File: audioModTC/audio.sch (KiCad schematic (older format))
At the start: 39 parts

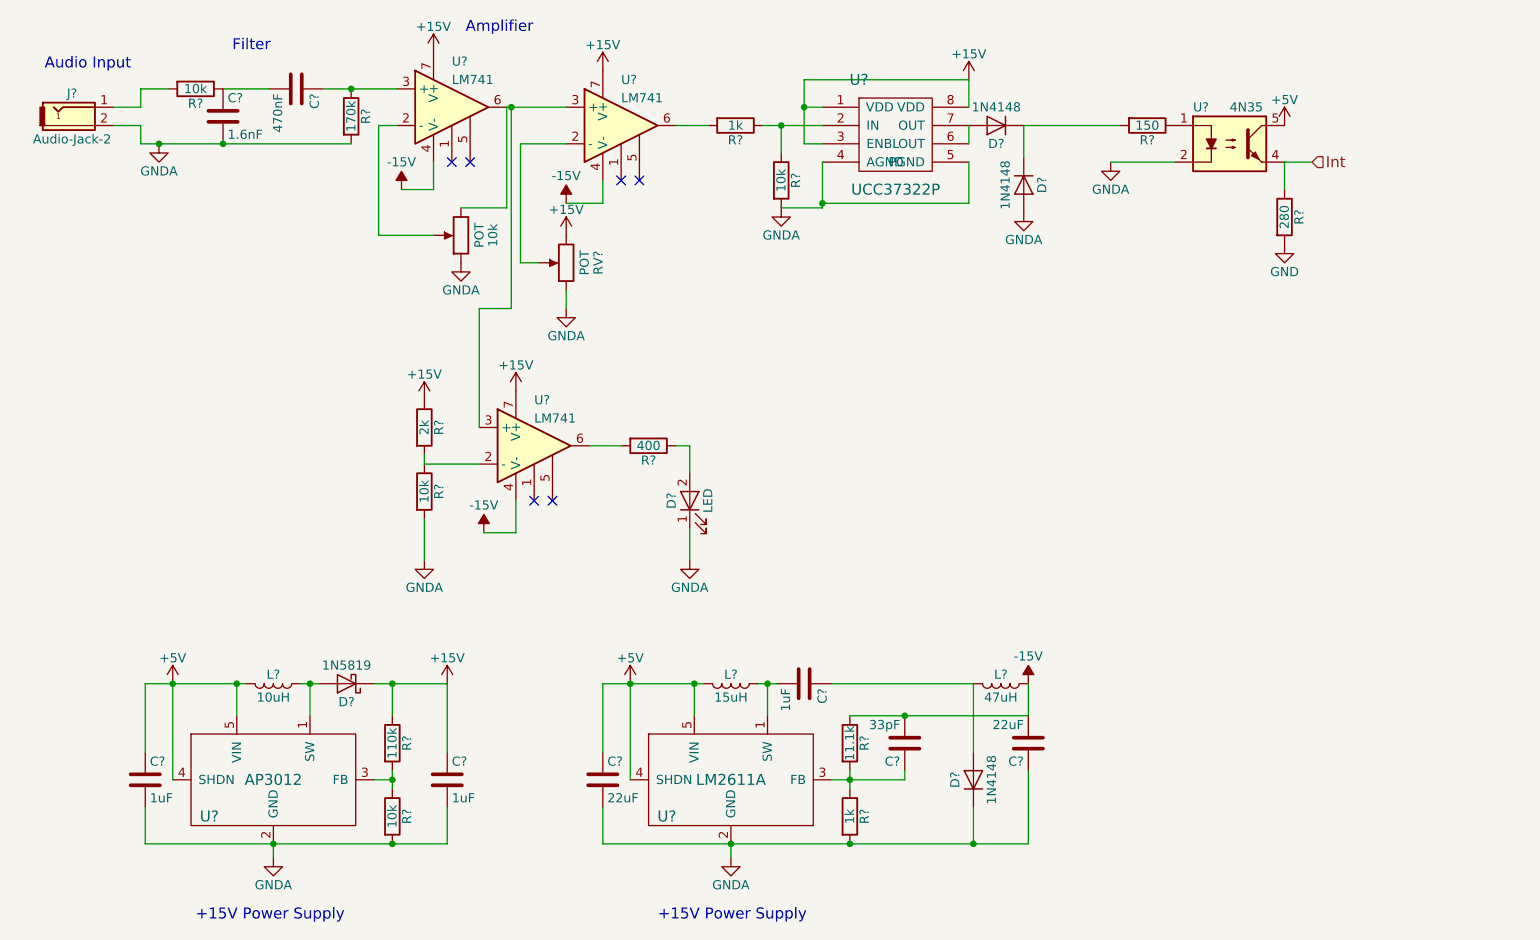
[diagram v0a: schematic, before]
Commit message: Made some footprints
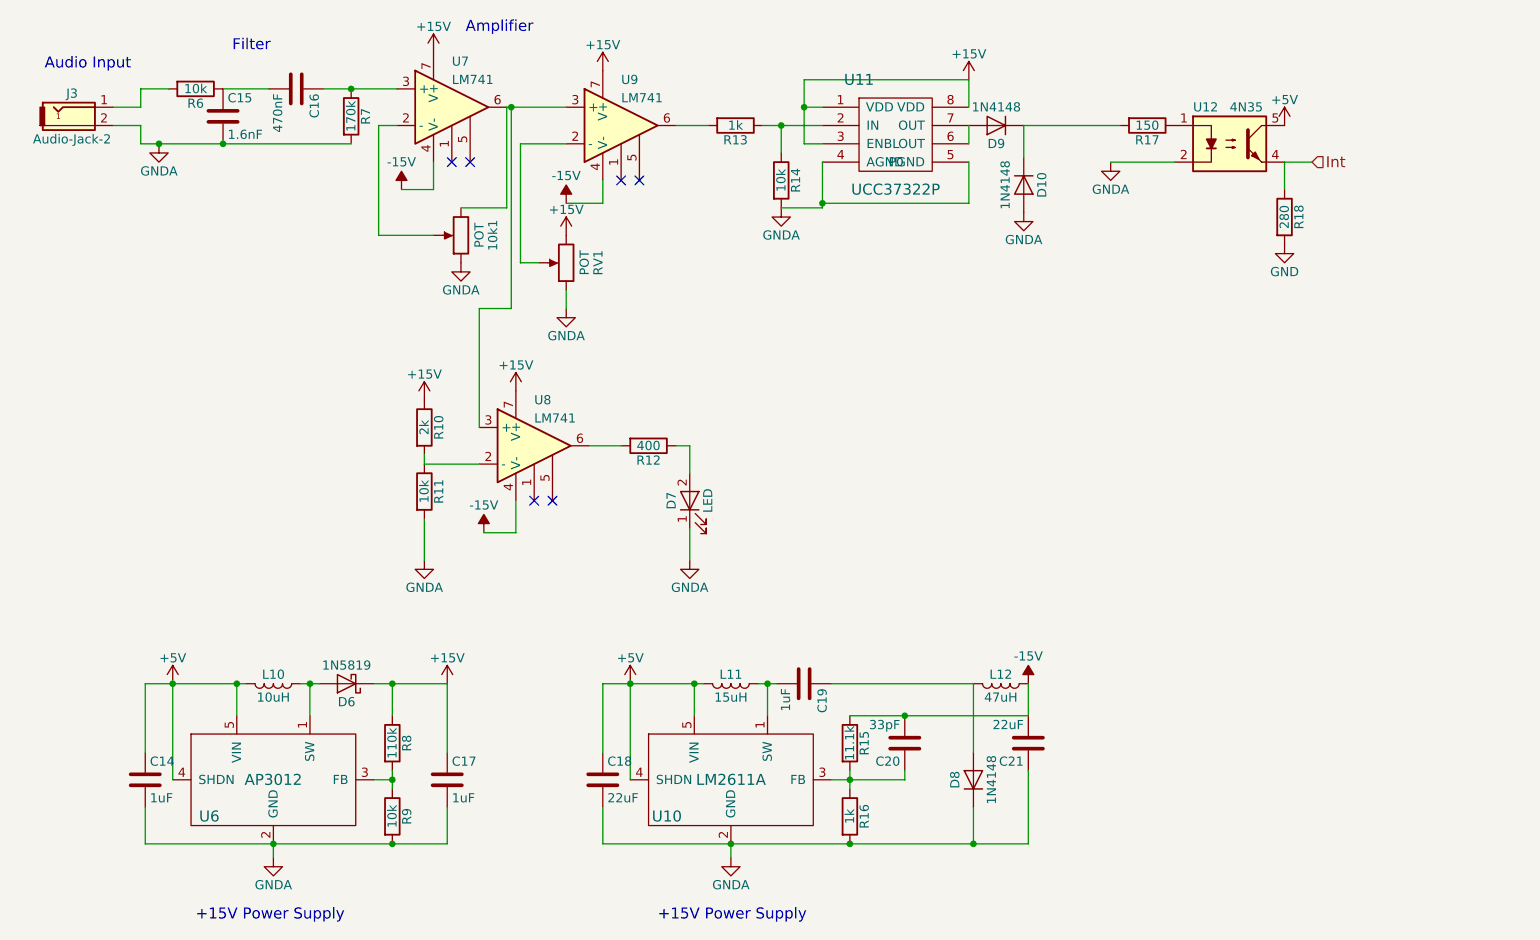
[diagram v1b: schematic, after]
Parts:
- C14, C15, C16, C17, C18, C19, C20, C21: renamed from C?; footprint (none) -> Capacitors_SMD:C_0603
- gave numbers to parts that had none: 30
- renumbered 10k to 10k1

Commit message: Assigned more footprints
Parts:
- D10, D8, D9: footprint (none) -> Diodes_SMD:D_SOD-323
- D6: footprint (none) -> Diodes_SMD:D_SOD-123
- D7: footprint (none) -> Diodes_SMD:D_0805
- J3: footprint (none) -> Custom:MJ1-2503A
- L10, L11, L12: footprint (none) -> Custom:L_1008
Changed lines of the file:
@@
 F 0 "D9" H 6925 2350 50  0000 C CNN
 F 1 "1N4148" H 6925 2150 50  0000 C CNN
-F 2 "" H 6925 2250 50  0001 C CNN
+F 2 "Diodes_SMD:D_SOD-323" H 6925 2250 50  0001 C CNN
 F 3 "" H 6925 2250 50  0001 C CNN
 	1    6925 2250
@@
 F 0 "D10" H 7075 2675 50  0000 C CNN
 F 1 "1N4148" H 7075 2475 50  0000 C CNN
-F 2 "" H 7075 2575 50  0001 C CNN
+F 2 "Diodes_SMD:D_SOD-323" H 7075 2575 50  0001 C CNN
 F 3 "" H 7075 2575 50  0001 C CNN
 	1    7075 2575
@@
 F 0 "D7" H 5250 4400 50  0000 C CNN
 F 1 "LED" H 5250 4200 50  0000 C CNN
-F 2 "" H 5250 4300 50  0001 C CNN
+F 2 "Diodes_SMD:D_0805" H 5250 4300 50  0001 C CNN
 F 3 "" H 5250 4300 50  0001 C CNN
 	1    5250 4300
@@
 F 0 "L10" V 2925 5300 50  0000 C CNN
 F 1 "10uH" V 3050 5300 50  0000 C CNN
-F 2 "" H 2975 5300 50  0001 C CNN
+F 2 "Custom:L_1008" H 2975 5300 50  0001 C CNN
 F 3 "" H 2975 5300 50  0001 C CNN
 	1    2975 5300
@@
 F 0 "D6" H 3375 5400 50  0000 C CNN
 F 1 "1N5819" H 3375 5200 50  0000 C CNN
-F 2 "" H 3375 5300 50  0001 C CNN
+F 2 "Diodes_SMD:D_SOD-123" H 3375 5300 50  0001 C CNN
 F 3 "" H 3375 5300 50  0001 C CNN
 	1    3375 5300
@@
 F 0 "L11" V 5425 5300 50  0000 C CNN
 F 1 "15uH" V 5550 5300 50  0000 C CNN
-F 2 "" H 5475 5300 50  0001 C CNN
+F 2 "Custom:L_1008" H 5475 5300 50  0001 C CNN
 F 3 "" H 5475 5300 50  0001 C CNN
 	1    5475 5300
@@
 F 0 "D8" H 6800 5925 50  0000 C CNN
 F 1 "1N4148" H 6800 5725 50  0000 C CNN
-F 2 "" H 6800 5825 50  0001 C CNN
+F 2 "Diodes_SMD:D_SOD-323" H 6800 5825 50  0001 C CNN
 F 3 "" H 6800 5825 50  0001 C CNN
 	1    6800 5825
@@
 F 0 "L12" V 6900 5300 50  0000 C CNN
 F 1 "47uH" V 7025 5300 50  0000 C CNN
-F 2 "" H 6950 5300 50  0001 C CNN
+F 2 "Custom:L_1008" H 6950 5300 50  0001 C CNN
 F 3 "" H 6950 5300 50  0001 C CNN
 	1    6950 5300
@@
 F 0 "J3" H 1875 2225 50  0000 C CNN
 F 1 "Audio-Jack-2" H 1875 1975 50  0000 C CNN
-F 2 "" H 2150 2150 50  0001 C CNN
+F 2 "Custom:MJ1-2503A" H 2150 2150 50  0001 C CNN
 F 3 "" H 2150 2150 50  0001 C CNN
 	1    1900 2150

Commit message: Made more footprints
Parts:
- R10, R11, R12, R13, R14, R15, R16, R17, R18, R6, R7, R8, R9: footprint (none) -> Resistors_SMD:R_0603
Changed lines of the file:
@@
 F 0 "R6" V 2630 2050 50  0000 C CNN
 F 1 "10k" V 2550 2050 50  0000 C CNN
-F 2 "" V 2480 2050 50  0001 C CNN
+F 2 "Resistors_SMD:R_0603" V 2480 2050 50  0001 C CNN
 F 3 "" H 2550 2050 50  0001 C CNN
 	1    2550 2050
@@
 F 0 "R7" V 3480 2200 50  0000 C CNN
 F 1 "170k" V 3400 2200 50  0000 C CNN
-F 2 "" V 3330 2200 50  0001 C CNN
+F 2 "Resistors_SMD:R_0603" V 3330 2200 50  0001 C CNN
 F 3 "" H 3400 2200 50  0001 C CNN
 	1    3400 2200
@@
 F 0 "R13" V 5580 2250 50  0000 C CNN
 F 1 "1k" V 5500 2250 50  0000 C CNN
-F 2 "" V 5430 2250 50  0001 C CNN
+F 2 "Resistors_SMD:R_0603" V 5430 2250 50  0001 C CNN
 F 3 "" H 5500 2250 50  0001 C CNN
 	1    5500 2250
@@
 F 0 "R14" V 5830 2550 50  0000 C CNN
 F 1 "10k" V 5750 2550 50  0000 C CNN
-F 2 "" V 5680 2550 50  0001 C CNN
+F 2 "Resistors_SMD:R_0603" V 5680 2550 50  0001 C CNN
 F 3 "" H 5750 2550 50  0001 C CNN
 	1    5750 2550
@@
 F 0 "R17" V 7830 2250 50  0000 C CNN
 F 1 "150" V 7750 2250 50  0000 C CNN
-F 2 "" V 7680 2250 50  0001 C CNN
+F 2 "Resistors_SMD:R_0603" V 7680 2250 50  0001 C CNN
 F 3 "" H 7750 2250 50  0001 C CNN
 	1    7750 2250
@@
 F 0 "R18" V 8580 2750 50  0000 C CNN
 F 1 "280" V 8500 2750 50  0000 C CNN
-F 2 "" V 8430 2750 50  0001 C CNN
+F 2 "Resistors_SMD:R_0603" V 8430 2750 50  0001 C CNN
 F 3 "" H 8500 2750 50  0001 C CNN
 	1    8500 2750
@@
 F 0 "R10" V 3880 3900 50  0000 C CNN
 F 1 "2k" V 3800 3900 50  0000 C CNN
-F 2 "" V 3730 3900 50  0001 C CNN
+F 2 "Resistors_SMD:R_0603" V 3730 3900 50  0001 C CNN
 F 3 "" H 3800 3900 50  0001 C CNN
 	1    3800 3900
@@
 F 0 "R11" V 3880 4250 50  0000 C CNN
 F 1 "10k" V 3800 4250 50  0000 C CNN
-F 2 "" V 3730 4250 50  0001 C CNN
+F 2 "Resistors_SMD:R_0603" V 3730 4250 50  0001 C CNN
 F 3 "" H 3800 4250 50  0001 C CNN
 	1    3800 4250
@@
 F 0 "R12" V 5105 4000 50  0000 C CNN
 F 1 "400" V 5025 4000 50  0000 C CNN
-F 2 "" V 4955 4000 50  0001 C CNN
+F 2 "Resistors_SMD:R_0603" V 4955 4000 50  0001 C CNN
 F 3 "" H 5025 4000 50  0001 C CNN
 	1    5025 4000
@@
 F 0 "R8" V 3705 5625 50  0000 C CNN
 F 1 "110k" V 3625 5625 50  0000 C CNN
-F 2 "" V 3555 5625 50  0001 C CNN
+F 2 "Resistors_SMD:R_0603" V 3555 5625 50  0001 C CNN
 F 3 "" H 3625 5625 50  0001 C CNN
 	1    3625 5625
@@
 F 0 "R9" V 3705 6025 50  0000 C CNN
 F 1 "10k" V 3625 6025 50  0000 C CNN
-F 2 "" V 3555 6025 50  0001 C CNN
+F 2 "Resistors_SMD:R_0603" V 3555 6025 50  0001 C CNN
 F 3 "" H 3625 6025 50  0001 C CNN
 	1    3625 6025
@@
 F 0 "R15" V 6205 5625 50  0000 C CNN
 F 1 "11.1k" V 6125 5625 50  0000 C CNN
-F 2 "" V 6055 5625 50  0001 C CNN
+F 2 "Resistors_SMD:R_0603" V 6055 5625 50  0001 C CNN
 F 3 "" H 6125 5625 50  0001 C CNN
 	1    6125 5625
@@
 F 0 "R16" V 6205 6025 50  0000 C CNN
 F 1 "1k" V 6125 6025 50  0000 C CNN
-F 2 "" V 6055 6025 50  0001 C CNN
+F 2 "Resistors_SMD:R_0603" V 6055 6025 50  0001 C CNN
 F 3 "" H 6125 6025 50  0001 C CNN
 	1    6125 6025

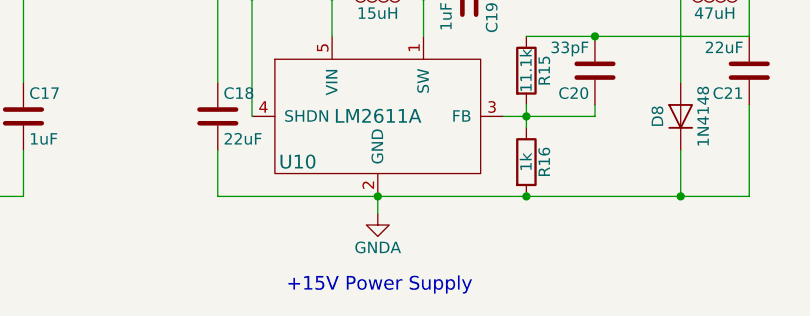
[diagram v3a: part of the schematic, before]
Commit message: Finished footprints
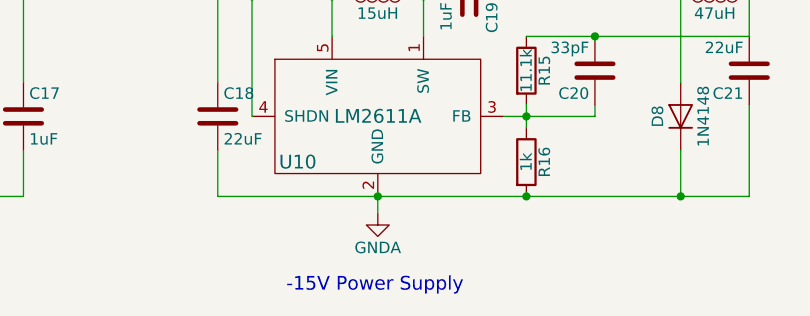
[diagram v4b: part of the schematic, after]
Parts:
- 10k1, RV1: footprint (none) -> Custom:PDB181-K220K-103B
- U10, U6: footprint (none) -> TO_SOT_Packages_SMD:SOT-23-5
- U11, U7, U8, U9: footprint (none) -> Housings_DIP:DIP-8_W7.62mm
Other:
- note added: "-15V Power Supply"
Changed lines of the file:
@@
 $EndComp
 $Comp
-L GNDA #PWR014
+L GNDA #PWR016
 U 1 1 5A4B5095
 P 2350 2350
-F 0 "#PWR014" H 2350 2100 50  0001 C CNN
+F 0 "#PWR016" H 2350 2100 50  0001 C CNN
 F 1 "GNDA" H 2350 2200 50  0000 C CNN
 F 2 "" H 2350 2350 50  0001 C CNN
@@
 F 0 "U7" H 3950 2400 50  0000 L CNN
 F 1 "LM741" H 3950 2300 50  0000 L CNN
-F 2 "" H 4000 2200 50  0001 C CNN
+F 2 "Housings_DIP:DIP-8_W7.62mm" H 4000 2200 50  0001 C CNN
 F 3 "" H 4100 2300 50  0001 C CNN
 	1    3950 2150
@@
 $EndComp
 $Comp
-L +15V #PWR015
+L +15V #PWR017
 U 1 1 5A4B51BF
 P 3850 1850
-F 0 "#PWR015" H 3850 1700 50  0001 C CNN
+F 0 "#PWR017" H 3850 1700 50  0001 C CNN
 F 1 "+15V" H 3850 1990 50  0000 C CNN
 F 2 "" H 3850 1850 50  0001 C CNN
@@
 $EndComp
 $Comp
-L -15V #PWR17
+L -15V #PWR18
 U 1 1 5A4B51DD
 P 3675 2600
-F 0 "#PWR17" H 3675 2700 50  0001 C CNN
+F 0 "#PWR18" H 3675 2700 50  0001 C CNN
 F 1 "-15V" H 3675 2750 50  0000 C CNN
 F 2 "" H 3675 2600 50  0001 C CNN
@@
 F 0 "10k1" V 3825 2850 50  0000 C CNN
 F 1 "POT" V 3900 2850 50  0000 C CNN
-F 2 "" H 4000 2850 50  0001 C CNN
+F 2 "Custom:PDB181-K220K-103B" H 4000 2850 50  0001 C CNN
 F 3 "" H 4000 2850 50  0001 C CNN
 	1    4000 2850
@@
 $EndComp
 $Comp
-L GNDA #PWR016
+L GNDA #PWR018
 U 1 1 5A4B5315
 P 4000 3000
-F 0 "#PWR016" H 4000 2750 50  0001 C CNN
+F 0 "#PWR018" H 4000 2750 50  0001 C CNN
 F 1 "GNDA" H 4000 2850 50  0000 C CNN
 F 2 "" H 4000 3000 50  0001 C CNN
@@
 F 0 "U9" H 4875 2500 50  0000 L CNN
 F 1 "LM741" H 4875 2400 50  0000 L CNN
-F 2 "" H 4925 2300 50  0001 C CNN
+F 2 "Housings_DIP:DIP-8_W7.62mm" H 4925 2300 50  0001 C CNN
 F 3 "" H 5025 2400 50  0001 C CNN
 	1    4875 2250
@@
 $EndComp
 $Comp
-L +15V #PWR017
+L +15V #PWR019
 U 1 1 5A4B53D4
 P 4775 1950
-F 0 "#PWR017" H 4775 1800 50  0001 C CNN
+F 0 "#PWR019" H 4775 1800 50  0001 C CNN
 F 1 "+15V" H 4775 2090 50  0000 C CNN
 F 2 "" H 4775 1950 50  0001 C CNN
@@
 $EndComp
 $Comp
-L -15V #PWR25
+L -15V #PWR26
 U 1 1 5A4B53F4
 P 4575 2675
-F 0 "#PWR25" H 4575 2775 50  0001 C CNN
+F 0 "#PWR26" H 4575 2775 50  0001 C CNN
 F 1 "-15V" H 4575 2825 50  0000 C CNN
 F 2 "" H 4575 2675 50  0001 C CNN
@@
 F 0 "RV1" V 4400 3000 50  0000 C CNN
 F 1 "POT" V 4475 3000 50  0000 C CNN
-F 2 "" H 4575 3000 50  0001 C CNN
+F 2 "Custom:PDB181-K220K-103B" H 4575 3000 50  0001 C CNN
 F 3 "" H 4575 3000 50  0001 C CNN
 	1    4575 3000
@@
 $EndComp
 $Comp
-L +15V #PWR018
+L +15V #PWR020
 U 1 1 5A4BBE9C
 P 4575 2850
-F 0 "#PWR018" H 4575 2700 50  0001 C CNN
+F 0 "#PWR020" H 4575 2700 50  0001 C CNN
 F 1 "+15V" H 4575 2990 50  0000 C CNN
 F 2 "" H 4575 2850 50  0001 C CNN
@@
 $EndComp
 $Comp
-L GNDA #PWR019
+L GNDA #PWR021
 U 1 1 5A4BBEC0
 P 4575 3250
-F 0 "#PWR019" H 4575 3000 50  0001 C CNN
+F 0 "#PWR021" H 4575 3000 50  0001 C CNN
 F 1 "GNDA" H 4575 3100 50  0000 C CNN
 F 2 "" H 4575 3250 50  0001 C CNN
@@
 F 0 "U11" H 6175 2600 60  0000 C CNN
 F 1 "UCC37322P" H 6375 2000 60  0000 C CNN
-F 2 "" H 6325 2300 60  0001 C CNN
+F 2 "Housings_DIP:DIP-8_W7.62mm" H 6325 2300 60  0001 C CNN
 F 3 "" H 6325 2300 60  0001 C CNN
 	1    6375 2300
@@
 	5875 2150 5975 2150
 $Comp
-L +15V #PWR020
+L +15V #PWR022
 U 1 1 5A4BC5F0
 P 6775 2000
-F 0 "#PWR020" H 6775 1850 50  0001 C CNN
+F 0 "#PWR022" H 6775 1850 50  0001 C CNN
 F 1 "+15V" H 6775 2140 50  0000 C CNN
 F 2 "" H 6775 2000 50  0001 C CNN
@@
 Connection ~ 5875 2150
 $Comp
-L GNDA #PWR021
+L GNDA #PWR023
 U 1 1 5A4BC691
 P 5750 2700
-F 0 "#PWR021" H 5750 2450 50  0001 C CNN
+F 0 "#PWR023" H 5750 2450 50  0001 C CNN
 F 1 "GNDA" H 5750 2550 50  0000 C CNN
 F 2 "" H 5750 2700 50  0001 C CNN
@@
 $EndComp
 $Comp
-L GNDA #PWR022
+L GNDA #PWR024
 U 1 1 5A4BC95E
 P 7075 2725
-F 0 "#PWR022" H 7075 2475 50  0001 C CNN
+F 0 "#PWR024" H 7075 2475 50  0001 C CNN
 F 1 "GNDA" H 7075 2575 50  0000 C CNN
 F 2 "" H 7075 2725 50  0001 C CNN
@@
 $EndComp
 $Comp
-L +5V #PWR023
+L +5V #PWR025
 U 1 1 5A4BD5E0
 P 8500 2250
-F 0 "#PWR023" H 8500 2100 50  0001 C CNN
+F 0 "#PWR025" H 8500 2100 50  0001 C CNN
 F 1 "+5V" H 8500 2390 50  0000 C CNN
 F 2 "" H 8500 2250 50  0001 C CNN
@@
 $EndComp
 $Comp
-L GNDA #PWR024
+L GNDA #PWR026
 U 1 1 5A4BDE28
 P 7550 2450
-F 0 "#PWR024" H 7550 2200 50  0001 C CNN
+F 0 "#PWR026" H 7550 2200 50  0001 C CNN
 F 1 "GNDA" H 7550 2300 50  0000 C CNN
 F 2 "" H 7550 2450 50  0001 C CNN
@@
 	8500 2450 8650 2450
 $Comp
-L GND #PWR025
+L GND #PWR027
 U 1 1 5A4C09BC
 P 8500 2900
-F 0 "#PWR025" H 8500 2650 50  0001 C CNN
+F 0 "#PWR027" H 8500 2650 50  0001 C CNN
 F 1 "GND" H 8500 2750 50  0000 C CNN
 F 2 "" H 8500 2900 50  0001 C CNN
@@
 F 0 "U8" H 4400 4250 50  0000 L CNN
 F 1 "LM741" H 4400 4150 50  0000 L CNN
-F 2 "" H 4450 4050 50  0001 C CNN
+F 2 "Housings_DIP:DIP-8_W7.62mm" H 4450 4050 50  0001 C CNN
 F 3 "" H 4550 4150 50  0001 C CNN
 	1    4400 4000
@@
 $EndComp
 $Comp
-L +15V #PWR026
+L +15V #PWR028
 U 1 1 5A4C5AB1
 P 4300 3700
-F 0 "#PWR026" H 4300 3550 50  0001 C CNN
+F 0 "#PWR028" H 4300 3550 50  0001 C CNN
 F 1 "+15V" H 4300 3840 50  0000 C CNN
 F 2 "" H 4300 3700 50  0001 C CNN
@@
 $EndComp
 $Comp
-L -15V #PWR23
+L -15V #PWR24
 U 1 1 5A4C5AEF
 P 4125 4475
-F 0 "#PWR23" H 4125 4575 50  0001 C CNN
+F 0 "#PWR24" H 4125 4575 50  0001 C CNN
 F 1 "-15V" H 4125 4625 50  0000 C CNN
 F 2 "" H 4125 4475 50  0001 C CNN
@@
 $EndComp
 $Comp
-L +15V #PWR027
+L +15V #PWR029
 U 1 1 5A4C6733
 P 3800 3750
-F 0 "#PWR027" H 3800 3600 50  0001 C CNN
+F 0 "#PWR029" H 3800 3600 50  0001 C CNN
 F 1 "+15V" H 3800 3890 50  0000 C CNN
 F 2 "" H 3800 3750 50  0001 C CNN
@@
 	3800 4400 3800 4625
 $Comp
-L GNDA #PWR028
+L GNDA #PWR030
 U 1 1 5A4C6A16
 P 3800 4625
-F 0 "#PWR028" H 3800 4375 50  0001 C CNN
+F 0 "#PWR030" H 3800 4375 50  0001 C CNN
 F 1 "GNDA" H 3800 4475 50  0000 C CNN
 F 2 "" H 3800 4625 50  0001 C CNN
@@
 	5250 4000 5250 4150
 $Comp
-L GNDA #PWR029
+L GNDA #PWR031
 U 1 1 5A4C7095
 P 5250 4625
-F 0 "#PWR029" H 5250 4375 50  0001 C CNN
+F 0 "#PWR031" H 5250 4375 50  0001 C CNN
 F 1 "GNDA" H 5250 4475 50  0000 C CNN
 F 2 "" H 5250 4625 50  0001 C CNN
@@
 F 0 "U6" H 2625 5625 60  0000 C CNN
 F 1 "AP3012" H 2975 5825 60  0000 C CNN
-F 2 "" H 2975 5825 60  0001 C CNN
+F 2 "TO_SOT_Packages_SMD:SOT-23-5" H 2975 5825 60  0001 C CNN
 F 3 "" H 2975 5825 60  0001 C CNN
 	1    2975 5825
@@
 Connection ~ 2775 5300
 $Comp
-L +5V #PWR030
+L +5V #PWR032
 U 1 1 5A4CBBDD
 P 2425 5300
-F 0 "#PWR030" H 2425 5150 50  0001 C CNN
+F 0 "#PWR032" H 2425 5150 50  0001 C CNN
 F 1 "+5V" H 2425 5440 50  0000 C CNN
 F 2 "" H 2425 5300 50  0001 C CNN
@@
 $EndComp
 $Comp
-L GNDA #PWR031
+L GNDA #PWR033
 U 1 1 5A4CD4FF
 P 2975 6250
-F 0 "#PWR031" H 2975 6000 50  0001 C CNN
+F 0 "#PWR033" H 2975 6000 50  0001 C CNN
 F 1 "GNDA" H 2975 6100 50  0000 C CNN
 F 2 "" H 2975 6250 50  0001 C CNN
@@
 Connection ~ 2425 5300
 $Comp
-L +15V #PWR032
+L +15V #PWR034
 U 1 1 5A4CED4C
 P 3925 5300
-F 0 "#PWR032" H 3925 5150 50  0001 C CNN
+F 0 "#PWR034" H 3925 5150 50  0001 C CNN
 F 1 "+15V" H 3925 5440 50  0000 C CNN
 F 2 "" H 3925 5300 50  0001 C CNN
@@
 F 0 "U10" H 5125 5625 60  0000 C CNN
 F 1 "LM2611A" H 5475 5825 60  0000 C CNN
-F 2 "" H 5475 5825 60  0001 C CNN
+F 2 "TO_SOT_Packages_SMD:SOT-23-5" H 5475 5825 60  0001 C CNN
 F 3 "" H 5475 5825 60  0001 C CNN
 	1    5475 5825
@@
 Connection ~ 5275 5300
 $Comp
-L +5V #PWR033
+L +5V #PWR035
 U 1 1 5A4E3125
 P 4925 5300
-F 0 "#PWR033" H 4925 5150 50  0001 C CNN
+F 0 "#PWR035" H 4925 5150 50  0001 C CNN
 F 1 "+5V" H 4925 5440 50  0000 C CNN
 F 2 "" H 4925 5300 50  0001 C CNN
@@
 $EndComp
 $Comp
-L GNDA #PWR034
+L GNDA #PWR036
 U 1 1 5A4E312B
 P 5475 6250
-F 0 "#PWR034" H 5475 6000 50  0001 C CNN
+F 0 "#PWR036" H 5475 6000 50  0001 C CNN
 F 1 "GNDA" H 5475 6100 50  0000 C CNN
 F 2 "" H 5475 6250 50  0001 C CNN
@@
 Connection ~ 6800 6175
 $Comp
-L -15V #PWR35
+L -15V #PWR36
 U 1 1 5A4F2130
 P 7100 5300
-F 0 "#PWR35" H 7100 5400 50  0001 C CNN
+F 0 "#PWR36" H 7100 5400 50  0001 C CNN
 F 1 "-15V" H 7100 5450 50  0000 C CNN
 F 2 "" H 7100 5300 50  0001 C CNN
@@
 +15V Power Supply
 Text Notes 5075 6600 0    60   ~ 0
-+15V Power Supply
+-15V Power Supply
 Text Notes 1725 1950 0    60   ~ 0
 Audio Input

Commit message: Finished footprints fo real
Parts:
- U12: footprint Housings_DIP:DIP-4_W7.62mm -> Housings_DIP:DIP-6_W7.62mm
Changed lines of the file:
@@
 $EndComp
 $Comp
-L -15V #PWR18
+L -15V #PWR19
 U 1 1 5A4B51DD
 P 3675 2600
-F 0 "#PWR18" H 3675 2700 50  0001 C CNN
+F 0 "#PWR19" H 3675 2700 50  0001 C CNN
 F 1 "-15V" H 3675 2750 50  0000 C CNN
 F 2 "" H 3675 2600 50  0001 C CNN
@@
 $EndComp
 $Comp
-L -15V #PWR26
+L -15V #PWR27
 U 1 1 5A4B53F4
 P 4575 2675
-F 0 "#PWR26" H 4575 2775 50  0001 C CNN
+F 0 "#PWR27" H 4575 2775 50  0001 C CNN
 F 1 "-15V" H 4575 2825 50  0000 C CNN
 F 2 "" H 4575 2675 50  0001 C CNN
@@
 F 0 "U12" H 8000 2550 50  0000 L CNN
 F 1 "4N35" H 8200 2550 50  0000 L CNN
-F 2 "Housings_DIP:DIP-4_W7.62mm" H 8000 2150 50  0001 L CIN
+F 2 "Housings_DIP:DIP-6_W7.62mm" H 8000 2150 50  0001 L CIN
 F 3 "" H 8200 2250 50  0001 L CNN
 	1    8200 2350
@@
 $EndComp
 $Comp
-L -15V #PWR24
+L -15V #PWR25
 U 1 1 5A4C5AEF
 P 4125 4475
-F 0 "#PWR24" H 4125 4575 50  0001 C CNN
+F 0 "#PWR25" H 4125 4575 50  0001 C CNN
 F 1 "-15V" H 4125 4625 50  0000 C CNN
 F 2 "" H 4125 4475 50  0001 C CNN
@@
 Connection ~ 6800 6175
 $Comp
-L -15V #PWR36
+L -15V #PWR37
 U 1 1 5A4F2130
 P 7100 5300
-F 0 "#PWR36" H 7100 5400 50  0001 C CNN
+F 0 "#PWR37" H 7100 5400 50  0001 C CNN
 F 1 "-15V" H 7100 5450 50  0000 C CNN
 F 2 "" H 7100 5300 50  0001 C CNN
